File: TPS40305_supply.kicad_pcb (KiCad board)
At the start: 2 copper layers, 0 parts

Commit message: added footprints
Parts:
- added C1: 47uF, Capacitor_SMD:C_1210_3225Metric, F.Cu at (152.0, 110.1)
- added C10: 470pF, Capacitor_SMD:C_0805_2012Metric, F.Cu at (155.8, 113.7)
- added C11: 220uF, TPS40305_supply:CAP_2R5TPE220MAFB, F.Cu at (158.3, 88.0)
- added C12: 100uF, Capacitor_SMD:C_1206_3216Metric, F.Cu at (160.7, 102.5)
- added C2: 47uF, Capacitor_SMD:C_1210_3225Metric, F.Cu at (166.3, 103.0)
- added C3: 47uF, Capacitor_SMD:C_1210_3225Metric, F.Cu at (157.7, 110.1)
- added C4: 1uF, Capacitor_SMD:C_0805_2012Metric, F.Cu at (160.1, 105.7)
- added C5: 3.3nF, Capacitor_SMD:C_0402_1005Metric, F.Cu at (162.4, 113.2)
- added C6: 180pF, Capacitor_SMD:C_0805_2012Metric, F.Cu at (162.7, 108.7)
- added C7: 1.5nF, Capacitor_SMD:C_0805_2012Metric, F.Cu at (151.4, 113.7)
- added C8: 100nF, Capacitor_SMD:C_0402_1005Metric, F.Cu at (161.9, 111.2)
- added C9: 10uF, Capacitor_SMD:C_0805_2012Metric, F.Cu at (171.4, 102.4)
- added L1: 150nH, TPS40305_supply:FP1005R1-R15-R, F.Cu at (149.6, 89.9)
- added Q1: CSD16340Q3, TPS40305_supply:CSD16340Q3, F.Cu at (157.5, 92.9)
- added Q2: CSD17311Q5, TPS40305_supply:CSD17311Q5, F.Cu at (152.8, 104.0)
- added R1: 3.83k, Resistor_SMD:R_0402_1005Metric, F.Cu at (166.7, 106.1)
- added R2: 100k, Resistor_SMD:R_0402_1005Metric, F.Cu at (170.6, 104.9)
- added R3: 4.12k, Resistor_SMD:R_0402_1005Metric, F.Cu at (163.7, 106.1)
- added R4: 1.33k, Resistor_SMD:R_0402_1005Metric, F.Cu at (166.4, 108.1)
- added R5: 10k, Resistor_SMD:R_0402_1005Metric, F.Cu at (159.5, 113.2)
- added R6: 5.62k, Resistor_SMD:R_0402_1005Metric, F.Cu at (166.4, 110.1)
- added R7: 2k, TPS40305_supply:ST4ETB202, F.Cu at (170.5, 113.9)
- added U1: TPS40305, TPS40305_supply:TPS40305, F.Cu at (176.2, 111.6)

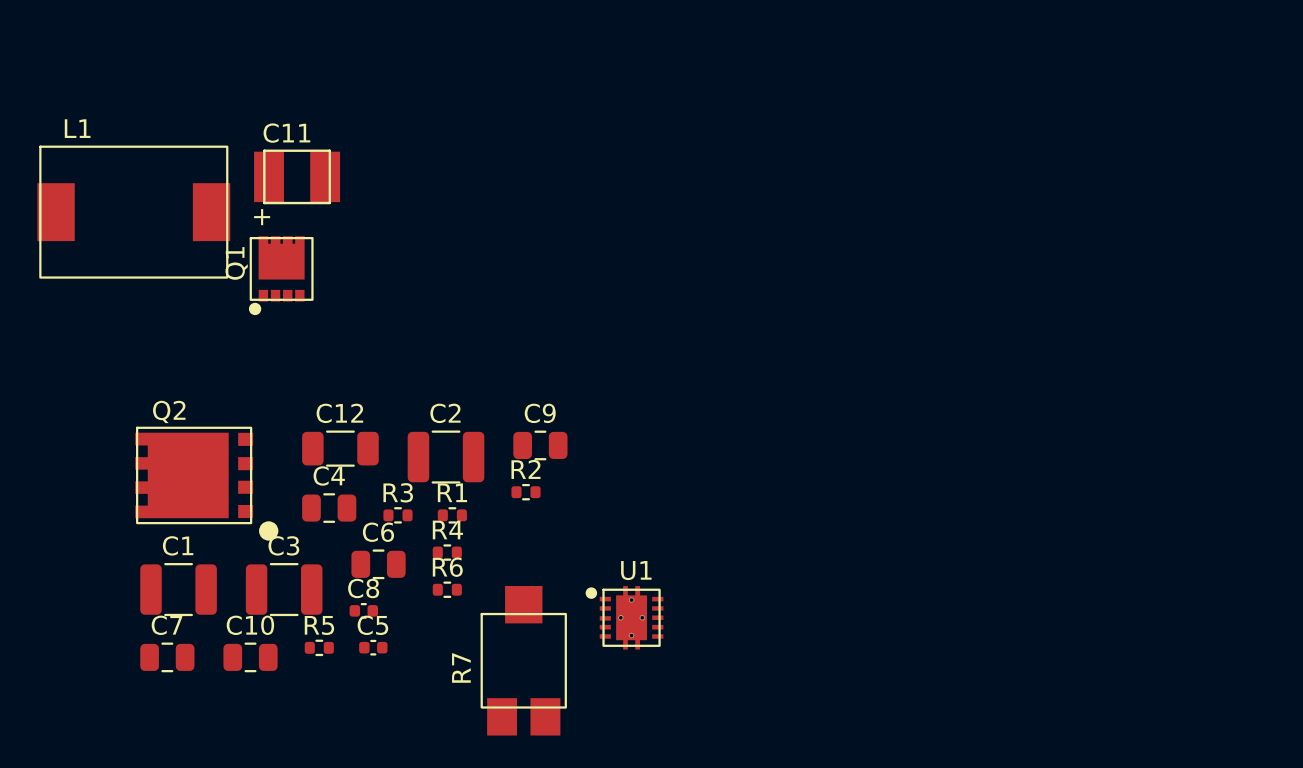
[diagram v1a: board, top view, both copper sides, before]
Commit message: added spade connectors ("we need a spade if we're gonna dig a pit.")
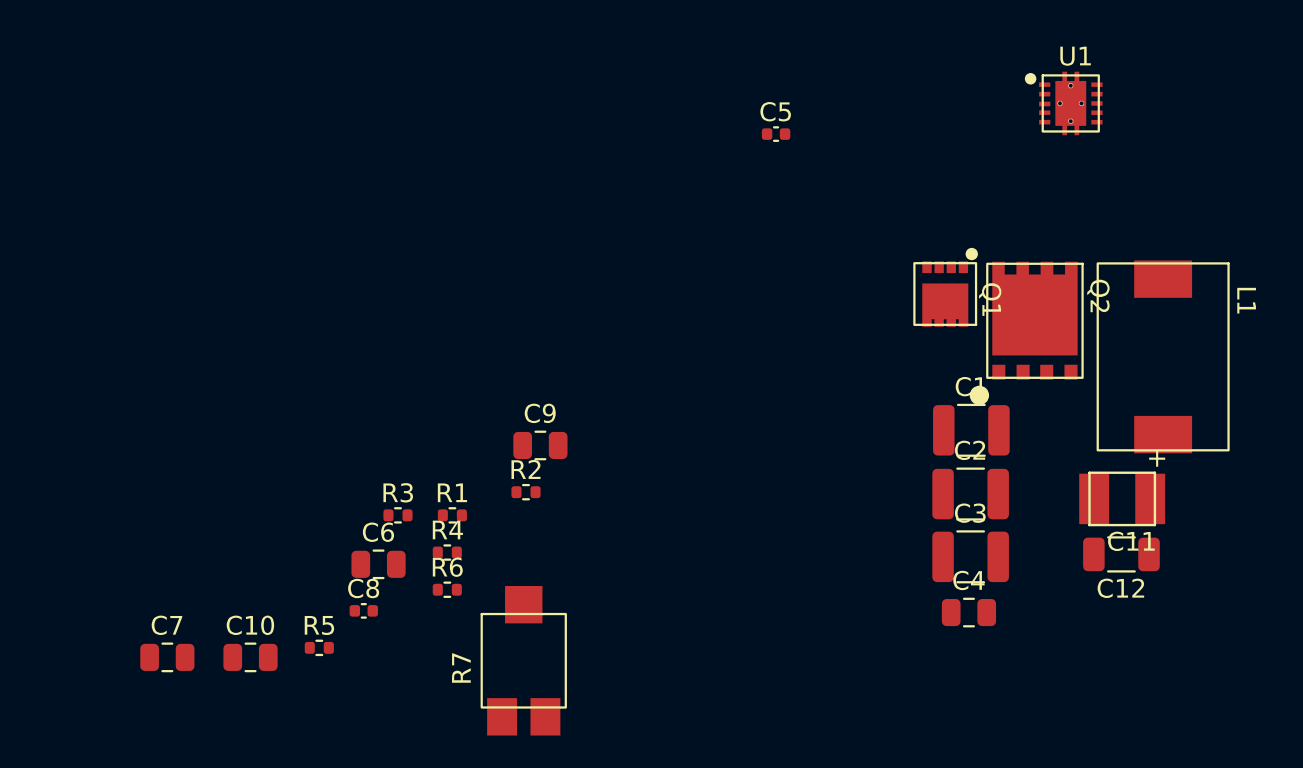
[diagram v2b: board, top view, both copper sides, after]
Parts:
- moved L1 55.6 mm to (204.7, 97.6), turned to -90 degrees
- moved C11 47.4 mm to (202.5, 105.2), turned to 180 degrees
- moved Q2 45.7 mm to (197.8, 95.7), turned to -90 degrees
- moved C1 43.3 mm to (194.4, 101.6)
- moved C12 42.2 mm to (202.4, 108.2), turned to 180 degrees
- moved C3 36.8 mm to (194.4, 108.3)
- moved U1 36.2 mm to (199.7, 84.1)
- moved Q1 35.5 mm to (193.0, 94.3), turned to 180 degrees
- moved C5 34.9 mm to (184.0, 85.7)
- moved C4 34.7 mm to (194.3, 111.3)
- moved C2 28.1 mm to (194.4, 105.0)
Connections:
- U1 pad 11: (no net) -> /GND

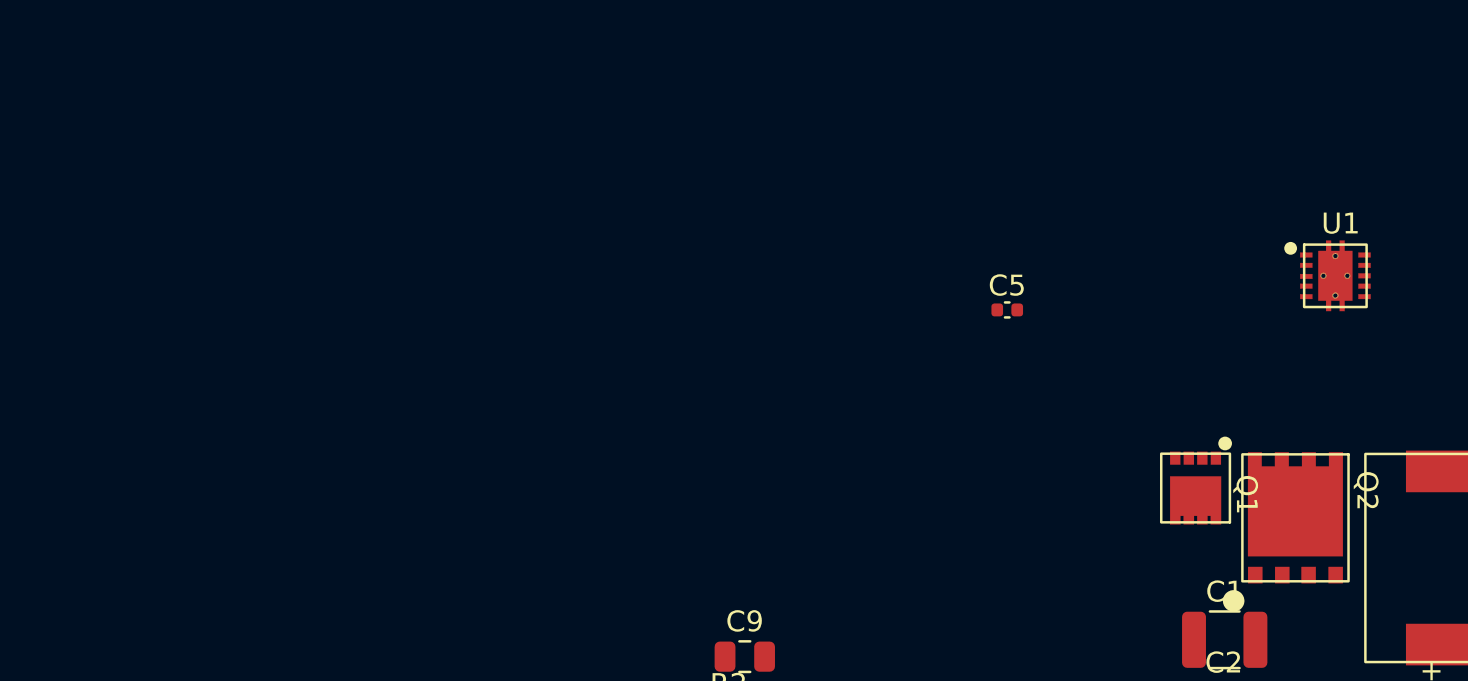
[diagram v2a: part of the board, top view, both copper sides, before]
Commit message: fixed problem with mosfet pad
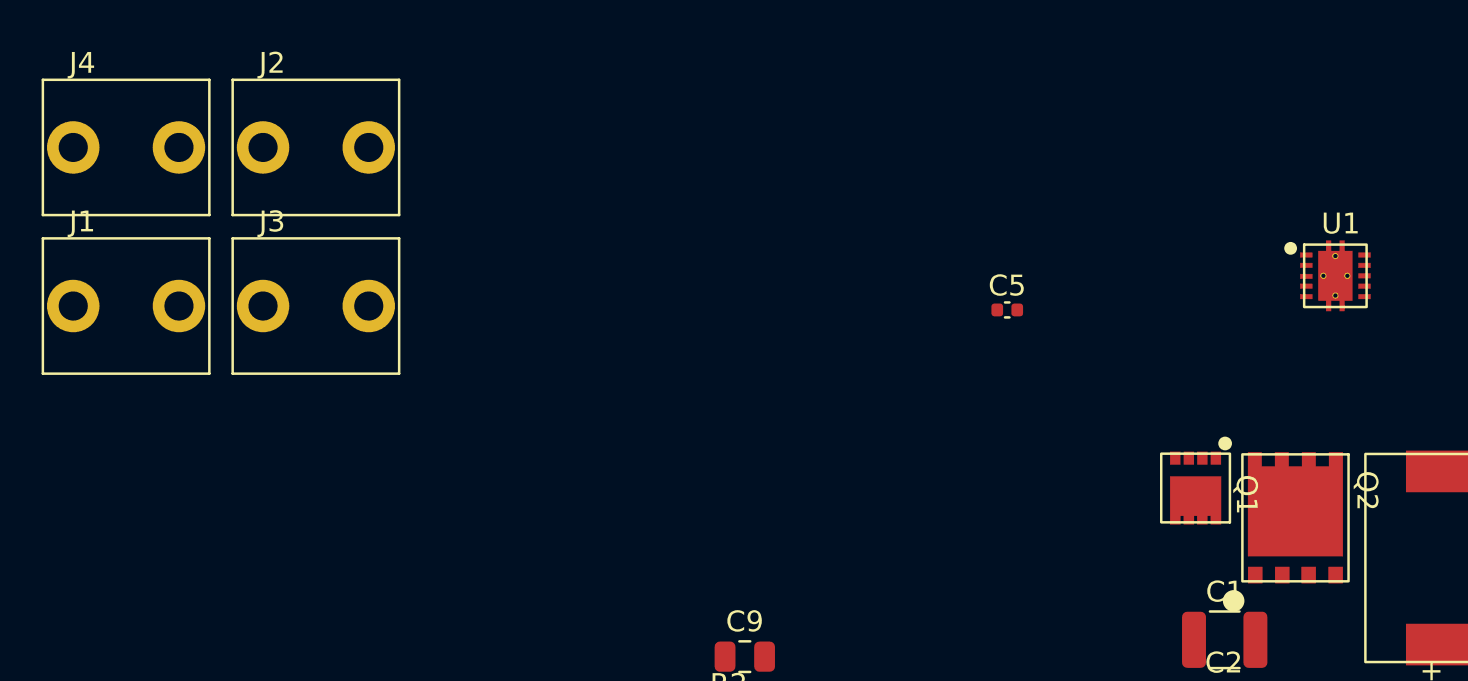
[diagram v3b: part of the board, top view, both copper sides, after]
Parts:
- added J1: Conn_01x01, TPS40305_supply:63862-1, F.Cu at (141.6, 85.5)
- added J2: Conn_01x01, TPS40305_supply:63862-1, F.Cu at (150.8, 77.9)
- added J3: Conn_01x01, TPS40305_supply:63862-1, F.Cu at (150.8, 85.5)
- added J4: Conn_01x01, TPS40305_supply:63862-1, F.Cu at (141.6, 77.9)

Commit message: more layout
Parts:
- moved J4 75.4 mm to (207.5, 114.7), turned to 90 degrees
- moved J3 70.1 mm to (214.5, 114.6), turned to 90 degrees
- moved J2 60.5 mm to (198.8, 114.6), turned to 90 degrees
- moved C7 59.7 mm to (198.9, 77.7), turned to 180 degrees
- moved J1 58.0 mm to (191.8, 114.6), turned to 90 degrees
- moved C10 48.7 mm to (191.9, 81.0), turned to 90 degrees
- moved C6 46.3 mm to (198.9, 79.9), turned to 180 degrees
- moved R5 44.1 mm to (189.5, 80.9)
- moved R2 43.3 mm to (206.7, 80.9)
- moved C8 43.2 mm to (198.2, 87.8)
- moved R3 41.3 mm to (200.7, 87.8)
- moved R1 40.2 mm to (196.1, 78.7), turned to -90 degrees
- moved C9 38.6 mm to (205.8, 84.9), turned to 90 degrees
- moved R6 38.3 mm to (189.5, 79.6), turned to 180 degrees
- moved R4 34.6 mm to (189.6, 82.4)
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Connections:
- net Net-(C8-Pad2) renamed /SW
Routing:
- net /VIN: track 0.00 -> 20.9 mm, vias 0 -> 2
- net Net-(Q2-Pad4): track 0.00 -> 16.9 mm, vias 0 -> 2
- net Net-(R2-Pad1): track 0.00 -> 8.25 mm
- net Net-(C5-Pad1): track 0.00 -> 7.78 mm
- net /SW: track 0.00 -> 6.98 mm
- net Net-(C10-Pad2): track 0.00 -> 3.07 mm
- net Net-(C6-Pad1): track 0.00 -> 3.02 mm
- added copper zone on F.Cu, net /GND
- added copper zone on F.Cu, net /SW
- added copper zone on F.Cu, net /VIN
- added copper zone on F.Cu, net /VOUT
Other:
- board outline added: 33.7 x 47.4 mm

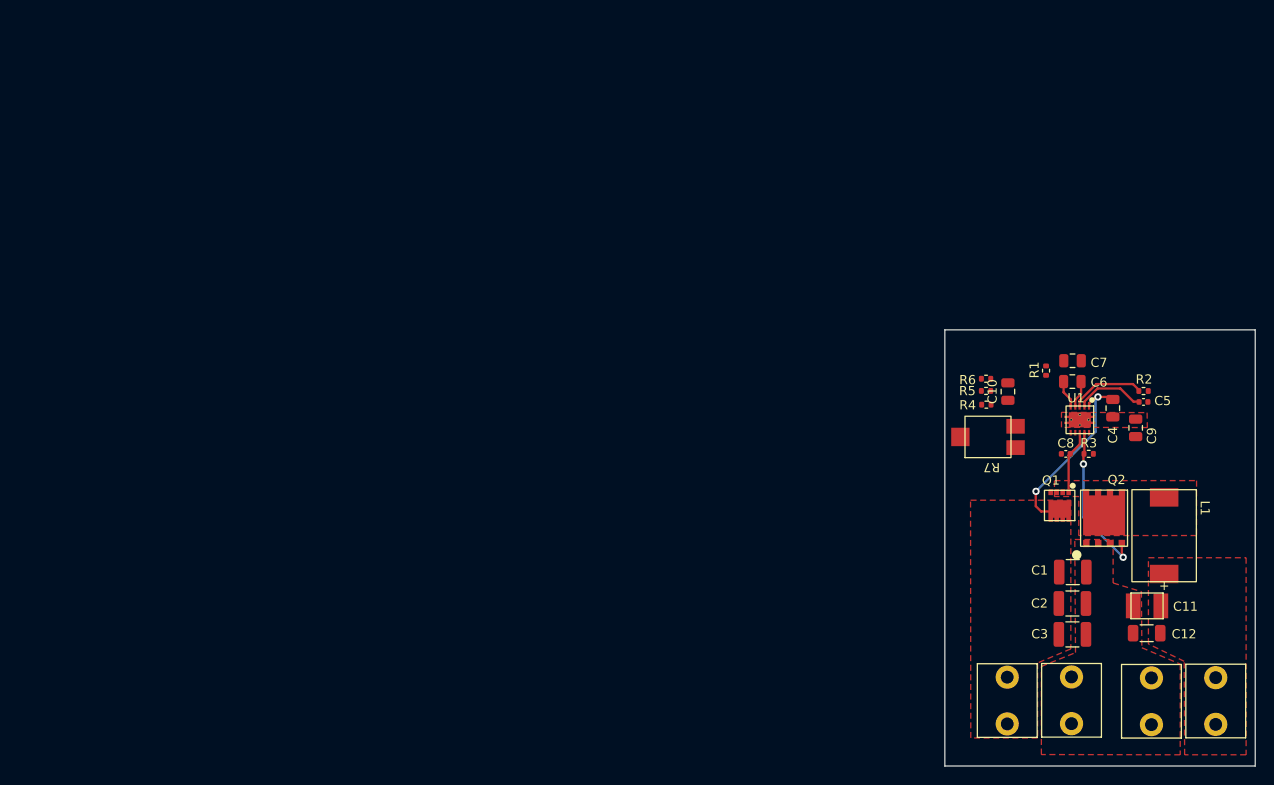
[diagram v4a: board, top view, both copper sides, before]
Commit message: initial layout and routing complete
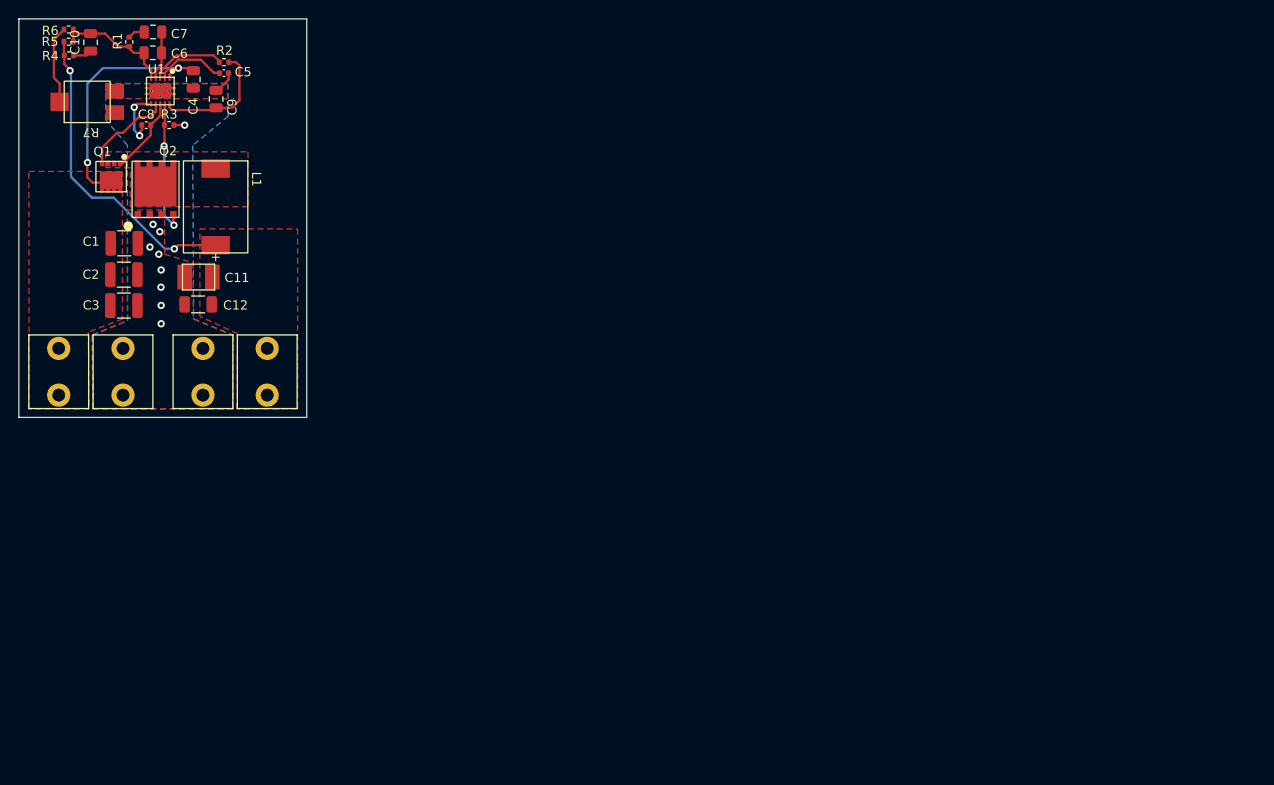
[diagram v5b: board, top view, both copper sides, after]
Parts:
- moved J4 109.1 mm to (104.4, 78.8)
- moved J3 109.1 mm to (111.4, 78.8)
- moved C2 109.1 mm to (95.9, 68.3)
- moved C3 109.1 mm to (95.9, 71.7)
- moved J1 109.1 mm to (88.8, 78.8)
- moved Q1 109.1 mm to (94.5, 57.6)
- moved Q2 109.1 mm to (99.3, 59.0)
- moved C1 109.1 mm to (95.9, 64.9)
- moved C11 109.1 mm to (104.0, 68.6)
- moved C12 109.1 mm to (103.9, 71.5)
- moved L1 109.1 mm to (105.8, 60.9)
- moved J2 109.1 mm to (95.8, 78.8)
- moved C10 106.7 mm to (92.2, 43.1)
- moved R6 106.7 mm to (89.9, 41.7)
- moved R4 106.7 mm to (89.9, 44.5)
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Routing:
- net /VOUT: track 0.00 -> 34.1 mm, vias 0 -> 2
- net Net-(C9-Pad1): track 0.00 -> 13.6 mm
- net Net-(C10-Pad2): track 3.07 -> 13.2 mm
- net Net-(Q1-Pad4): track 0.00 -> 10.0 mm
- net Net-(R6-Pad2): track 0.00 -> 8.58 mm
- net Net-(C8-Pad1): track 0.00 -> 6.56 mm, vias 0 -> 2
- net /VIN: track 20.9 -> 27.0 mm
- net /GND: track 0.00 -> 3.72 mm, vias 0 -> 9
- net Net-(C6-Pad1): track 3.02 -> 5.29 mm
- net Net-(Q2-Pad4): track 16.9 -> 14.8 mm
- net Net-(C10-Pad1): track 0.00 -> 2.03 mm
- net Net-(C7-Pad2): track 0.00 -> 1.86 mm
- net /SW: track 6.98 -> 8.43 mm
- added copper zone on B.Cu, net /GND
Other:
- board size 33.7 x 47.4 mm -> 31.3 x 43.3 mm

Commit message: added silkscreen and 3D part CAD files
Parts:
- added kibuzzard-633B51DB: G***, kibuzzard-633B51DB, F.Cu at (108.0, 77.7)
- added kibuzzard-633B5210: G***, kibuzzard-633B5210, F.Cu at (92.3, 77.7)
- moved J1 4.97 mm to (88.8, 83.8)
- moved J2 4.97 mm to (95.7, 83.8)
- moved J3 4.97 mm to (111.4, 83.8)
- moved J4 4.97 mm to (104.4, 83.8)
- moved L1 1.79 mm to (107.6, 60.8)
- moved R5 0.09 mm to (89.9, 43.1)
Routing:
- net /VOUT: track 34.1 -> 48.2 mm
- net Net-(Q2-Pad4): track 14.8 -> 15.9 mm
- net /GND: vias 9 -> 13
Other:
- board size 31.3 x 43.3 mm -> 31.3 x 48.4 mm
- board text added: "TPS40305 Supply R1"
